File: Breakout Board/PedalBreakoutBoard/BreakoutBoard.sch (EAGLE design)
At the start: 45 parts, among them J7 SMT GUITAR DC JACK, U1 ES_DAISY_SEED_REV4

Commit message: DP-16 - Working on board layout
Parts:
- removed J7: SMT GUITAR DC JACK, Electrosmith-Connectors:GUITAR_DC_JACK
- added PWR: (no value), SparkFun-Connectors:CONN_02
- renumbered R1 to L1, R10 to D21, R11 to D12, R12 to D11, R13 to 8T1, R14 to 8T2, R15 to 8T3, R16 to 8T4, R17 to 8T5, R18 to 8T6, R19 to 8T7, R2 to L2, R20 to 8T8, R3 to L3, R4 to S4, R5 to S3, R6 to S2, R7 to S1, R8 to L4, R9 to D22
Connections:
- net 1P8T_1: now also U1.GPIO31(USB_HS_D+); no longer U1.GPIO24(DAC1_OUT1)
- net 1P8T_2: now also U1.GPIO30(USB_HS_D_-); no longer U1.GPIO25(SAI2_MCLK_B)
- net 1P8T_3: now also U1.GPIO29(SAI2_SCK_B); no longer U1.GPIO26(SAI2_SD_B)
- net 1P8T_4: now also U1.GPIO28(SAI2_FS_B); no longer U1.GPIO27(SAI2_SD_A)
- net 1P8T_5: now also U1.GPIO27(SAI2_SD_A); no longer U1.GPIO28(SAI2_FS_B)
- net 1P8T_6: now also U1.GPIO26(SAI2_SD_B); no longer U1.GPIO29(SAI2_SCK_B)
- net 1P8T_7: now also U1.GPIO25(SAI2_MCLK_B); no longer U1.GPIO30(USB_HS_D_-)
- net 1P8T_8: now also U1.GPIO24(DAC1_OUT1); no longer U1.GPIO31(USB_HS_D+)
- net GND: now also PWR.1; no longer J7.GND
- net N$2: now also PWR.2; no longer J7.PIN

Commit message: DP-16 - Board layout REV-A
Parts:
- removed 1P8T: (no value), SparkFun-Connectors:CONN_09
- removed GPIOS: (no value), SparkFun-Connectors:CONN_07
- removed IN_L, IN_R, LED1, LED2, LED3, LED4, OUT_L, OUT_R, SPST1, SPST2, SPST3, SPST4: (no value), SparkFun-Connectors:CONN_02
- removed POT1, POT2, POT3, POT4, SPDT1, SPDT2: (no value), SparkFun-Connectors:CONN_03
- added 1P8T_GPIO: (no value), SparkFun-Connectors:CONN_08"
- added 1P8T_PWR: (no value), SparkFun-Connectors:CONN_01
- added AUDIO, EX_GND, EX_PWR: (no value), SparkFun-Connectors:CONN_04X2
- added EX_GPIOS: (no value), SparkFun-Connectors:CONN_07
- added LED_GND, LED_GPIO, POT_GND, POT_GPIO, POT_PWR, SPDT_GPIO, SPST_GPIO, SPST_PWR: (no value), SparkFun-Connectors:CONN_04
- added SPDT_PWR: (no value), SparkFun-Connectors:CONN_02
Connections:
- removed net GPIO10: GPIOS.6, U1.GPIO10(SPI1_MISO)
- removed net GPIO11: GPIOS.5, U1.GPIO11(SPI1_MOSI)
- removed net GPIO12: GPIOS.4, U1.GPIO12(I2C1_SCL)
- removed net GPIO13: GPIOS.3, U1.GPIO13(I2C1_SDA)
- removed net GPIO14: GPIOS.2, U1.GPIO14(USART1_TX)
- removed net GPIO15: GPIOS.1, U1.GPIO15(USART1_RX)
- removed net GPIO9: GPIOS.7, U1.GPIO9(SPI1_SCK)
- removed net N$6: L2.2, LED2.1
- removed net N$7: L3.2, LED3.1
- removed net N$8: L4.2, LED4.1
- new net GPIO1: EX_GPIOS.7, U1.GPIO1(USB_HS_ID)
- new net GPIO2: EX_GPIOS.6, U1.GPIO2(SDMMC1_D3)
- new net GPIO3: EX_GPIOS.5, U1.GPIO3(SDMMC1_D2)
- new net GPIO4: EX_GPIOS.4, U1.GPIO4(SDMMC1_D1)
- new net GPIO5: EX_GPIOS.3, U1.GPIO5(SDMMC1_D0)
- new net GPIO6: EX_GPIOS.2, U1.GPIO6(SDMMC1_CMD)
- new net GPIO7: EX_GPIOS.1, U1.GPIO7(SDMMC1_CK)
- new net N$1: L1.2, LED_GPIO.1
- new net N$3: L2.2, LED_GPIO.2
- new net N$4: L3.2, LED_GPIO.3
- net +3V3_A: now also 1P8T_PWR.1, EX_PWR.1, EX_PWR.2, EX_PWR.3, EX_PWR.4, EX_PWR.5, EX_PWR.6, EX_PWR.7, EX_PWR.8, POT_PWR.1, POT_PWR.2, POT_PWR.3, POT_PWR.4, SPDT_PWR.1, SPDT_PWR.2, SPST_PWR.1, SPST_PWR.2, SPST_PWR.3, SPST_PWR.4; no longer 1P8T.9, POT1.1, POT2.1, POT3.1, POT4.1, SPDT1.2, SPDT2.2, SPST1.1, SPST2.1, SPST3.1, SPST4.1
- net 1P8T_1: now also 1P8T_GPIO.1; no longer 1P8T.1
- net 1P8T_2: now also 1P8T_GPIO.2; no longer 1P8T.2
- net 1P8T_3: now also 1P8T_GPIO.3; no longer 1P8T.3
- net 1P8T_4: now also 1P8T_GPIO.4; no longer 1P8T.4
- net 1P8T_5: now also 1P8T_GPIO.5; no longer 1P8T.5
- net 1P8T_6: now also 1P8T_GPIO.6; no longer 1P8T.6
- net 1P8T_7: now also 1P8T_GPIO.7; no longer 1P8T.7
- net 1P8T_8: now also 1P8T_GPIO.8; no longer 1P8T.8
- net GND: now also AUDIO.1, AUDIO.3, AUDIO.5, AUDIO.7, EX_GND.1, EX_GND.2, EX_GND.3, EX_GND.4, EX_GND.5, EX_GND.6, EX_GND.7, EX_GND.8, LED_GND.1, LED_GND.2, LED_GND.3, LED_GND.4, POT_GND.1, POT_GND.2, POT_GND.3, POT_GND.4; no longer IN_L.1, IN_R.1, LED1.2, LED2.2, LED3.2, LED4.2, OUT_L.1, OUT_R.1, POT1.3, POT2.3, POT3.3, POT4.3
- net IN_L: now also AUDIO.2; no longer IN_L.2
- net IN_R: now also AUDIO.4; no longer IN_R.2
- net N$5: now also L4.2, LED_GPIO.4; no longer L1.2, LED1.1
- net OUT_L: now also AUDIO.6; no longer OUT_L.2
- net OUT_R: now also AUDIO.8; no longer OUT_R.2
- net POT1: now also POT_GPIO.1; no longer POT1.2
- net POT2: now also POT_GPIO.2; no longer POT2.2
- net POT3: now also POT_GPIO.3; no longer POT3.2
- net POT4: now also POT_GPIO.4; no longer POT4.2
- net SPDT1_1: now also SPDT_GPIO.4, U1.GPIO12(I2C1_SCL); no longer SPDT1.3, U1.GPIO5(SDMMC1_D0)
- net SPDT1_2: now also SPDT_GPIO.3, U1.GPIO13(I2C1_SDA); no longer SPDT1.1, U1.GPIO6(SDMMC1_CMD)
- net SPDT2_1: now also SPDT_GPIO.2, U1.GPIO14(USART1_TX); no longer SPDT2.3, U1.GPIO7(SDMMC1_CK)
- net SPDT2_2: now also SPDT_GPIO.1, U1.GPIO15(USART1_RX); no longer SPDT2.1, U1.GPIO8(SPI1_NSS)
- net SPST1: now also SPST_GPIO.4, U1.GPIO8(SPI1_NSS); no longer SPST1.2, U1.GPIO1(USB_HS_ID)
- net SPST2: now also SPST_GPIO.3, U1.GPIO9(SPI1_SCK); no longer SPST2.2, U1.GPIO2(SDMMC1_D3)
- net SPST3: now also SPST_GPIO.2, U1.GPIO10(SPI1_MISO); no longer SPST3.2, U1.GPIO3(SDMMC1_D2)
- net SPST4: now also SPST_GPIO.1, U1.GPIO11(SPI1_MOSI); no longer SPST4.2, U1.GPIO4(SDMMC1_D1)
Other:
- moved on the sheet: L1, L2, L3, L4

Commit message: DP-16 - Board layout REV-B
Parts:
- removed 1P8T_GPIO: (no value), SparkFun-Connectors:CONN_08"
- removed 8T1, 8T2, 8T3, 8T4: 10k, SparkFun-Resistors:10KOHM-HORIZ-1/4W-5%
- added HEX_GPIO: (no value), SparkFun-Connectors:CONN_04
- EX_GND, EX_PWR: device SparkFun-Connectors:CONN_04X2 -> SparkFun-Connectors:CONN_04
- EX_GPIOS: device SparkFun-Connectors:CONN_07 -> SparkFun-Connectors:CONN_04
- renumbered 1P8T_PWR to HEX_PWR
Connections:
- removed net 1P8T_1: 1P8T_GPIO.1, 8T1.2, U1.GPIO31(USB_HS_D+)
- removed net 1P8T_2: 1P8T_GPIO.2, 8T2.2, U1.GPIO30(USB_HS_D_-)
- removed net 1P8T_3: 1P8T_GPIO.3, 8T3.2, U1.GPIO29(SAI2_SCK_B)
- removed net 1P8T_4: 1P8T_GPIO.4, 8T4.2, U1.GPIO28(SAI2_FS_B)
- removed net 1P8T_5: 1P8T_GPIO.5, 8T5.2, U1.GPIO27(SAI2_SD_A)
- removed net 1P8T_6: 1P8T_GPIO.6, 8T6.2, U1.GPIO26(SAI2_SD_B)
- removed net 1P8T_7: 1P8T_GPIO.7, 8T7.2, U1.GPIO25(SAI2_MCLK_B)
- removed net 1P8T_8: 1P8T_GPIO.8, 8T8.2, U1.GPIO24(DAC1_OUT1)
- removed net GPIO5: EX_GPIOS.3, U1.GPIO5(SDMMC1_D0)
- removed net GPIO6: EX_GPIOS.2, U1.GPIO6(SDMMC1_CMD)
- removed net GPIO7: EX_GPIOS.1, U1.GPIO7(SDMMC1_CK)
- new net HEX_1: 8T5.2, HEX_GPIO.1, U1.GPIO30(USB_HS_D_-)
- new net HEX_2: 8T6.2, HEX_GPIO.2, U1.GPIO29(SAI2_SCK_B)
- new net HEX_3: 8T7.2, HEX_GPIO.3, U1.GPIO28(SAI2_FS_B)
- new net HEX_4: 8T8.2, HEX_GPIO.4, U1.GPIO27(SAI2_SD_A)
- net +3V3_A: no longer EX_PWR.5, EX_PWR.6, EX_PWR.7, EX_PWR.8
- net GND: no longer 8T1.1, 8T2.1, 8T3.1, 8T4.1, EX_GND.5, EX_GND.6, EX_GND.7, EX_GND.8
- net GPIO1: now also EX_GPIOS.4; no longer EX_GPIOS.7
- net GPIO2: now also EX_GPIOS.3; no longer EX_GPIOS.6
- net GPIO3: now also EX_GPIOS.2; no longer EX_GPIOS.5
- net GPIO4: now also EX_GPIOS.1; no longer EX_GPIOS.4
- net POT1: now also U1.GPIO24(DAC1_OUT1); no longer U1.GPIO23(DAC1_OUT2)
- net POT2: now also U1.GPIO23(DAC1_OUT2); no longer U1.GPIO22(ADC1_INP4)
- net POT3: now also U1.GPIO22(ADC1_INP4); no longer U1.GPIO21(ADC1_INP11)
- net POT4: now also U1.GPIO21(ADC1_INP11); no longer U1.GPIO20(ADC1_INP3)
- net SPDT1_1: now also U1.GPIO11(SPI1_MOSI); no longer U1.GPIO12(I2C1_SCL)
- net SPDT1_2: now also U1.GPIO12(I2C1_SCL); no longer U1.GPIO13(I2C1_SDA)
- net SPDT2_1: now also U1.GPIO13(I2C1_SDA); no longer U1.GPIO14(USART1_TX)
- net SPDT2_2: now also U1.GPIO14(USART1_TX); no longer U1.GPIO15(USART1_RX)
- net SPST1: now also U1.GPIO6(SDMMC1_CMD); no longer U1.GPIO8(SPI1_NSS)
- net SPST2: now also U1.GPIO7(SDMMC1_CK); no longer U1.GPIO9(SPI1_SCK)
- net SPST3: now also U1.GPIO8(SPI1_NSS); no longer U1.GPIO10(SPI1_MISO)
- net SPST4: now also U1.GPIO9(SPI1_SCK); no longer U1.GPIO11(SPI1_MOSI)

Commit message: DP-16 - Working on silkscreen and mounting holes
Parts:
- renumbered 8T5 to H1, 8T6 to H2, 8T7 to H3, 8T8 to H4, U1 to SEED

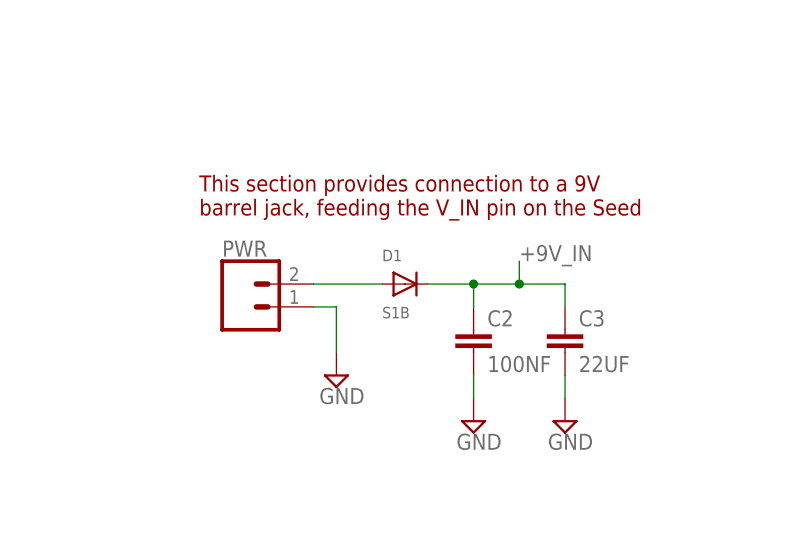
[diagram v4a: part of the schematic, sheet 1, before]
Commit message: DP-16 - Updating to through hole parts
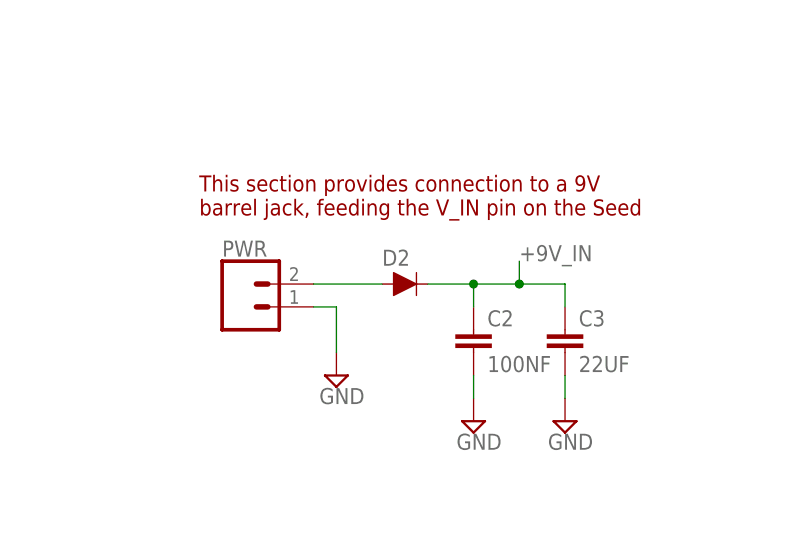
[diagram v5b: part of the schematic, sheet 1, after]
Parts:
- removed D1: S1B, Electrosmith-Semiconductors:S1B
- added D2: 200mA/100V/1V, SparkFun-DiscreteSemi:DIODE-1N4148
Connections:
- net +9V_IN: now also D2.C; no longer D1.C
- net N$2: now also D2.A; no longer D1.A
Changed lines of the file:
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@@
 <part name="C3" library="Electrosmith-Passives" deviceset="C-EU" device="C1206" package3d_urn="urn:adsk.eagle:package:23618/2" value="22UF"/>
 <part name="C2" library="Electrosmith-Passives" deviceset="C-EU" device="C0603" package3d_urn="urn:adsk.eagle:package:23616/2" value="100NF"/>
-<part name="D1" library="Electrosmith-Semiconductors" deviceset="S1B" device=""/>
 <part name="SUPPLY9" library="supply2" library_urn="urn:adsk.eagle:library:372" deviceset="GND" device=""/>
 <part name="SUPPLY10" library="supply2" library_urn="urn:adsk.eagle:library:372" deviceset="GND" device=""/>
@@
 <part name="EX_PWR" library="SparkFun-Connectors" library_urn="urn:adsk.eagle:library:513" deviceset="CONN_04" device="" package3d_urn="urn:adsk.eagle:package:38085/1"/>
 <part name="EX_GND" library="SparkFun-Connectors" library_urn="urn:adsk.eagle:library:513" deviceset="CONN_04" device="" package3d_urn="urn:adsk.eagle:package:38085/1"/>
+<part name="D2" library="SparkFun-DiscreteSemi" library_urn="urn:adsk.eagle:library:514" deviceset="DIODE" device="-1N4148" package3d_urn="urn:adsk.eagle:package:38452/1" value="200mA/100V/1V"/>
 </parts>
 <sheets>
@@
 <attribute name="VALUE" x="82.804" y="15.621" size="1.778" layer="96"/>
 </instance>
-<instance part="D1" gate="G$1" x="73.66" y="25.4" smashed="yes" grouprefs="POWER">
-<attribute name="NAME" x="71.12" y="27.94" size="1.27" layer="95"/>
-<attribute name="VALUE" x="71.12" y="21.59" size="1.27" layer="96"/>
-</instance>
 <instance part="SUPPLY9" gate="GND" x="66.04" y="15.24" smashed="yes" grouprefs="POWER">
 <attribute name="VALUE" x="64.135" y="12.065" size="1.778" layer="96"/>
@@
 <attribute name="VALUE" x="147.32" y="20.066" size="1.778" layer="96" font="vector" rot="R180"/>
 <attribute name="NAME" x="149.86" y="19.812" size="1.778" layer="95" font="vector" rot="R180"/>
+</instance>
+<instance part="D2" gate="G$1" x="73.66" y="25.4" smashed="yes">
+<attribute name="NAME" x="71.12" y="27.432" size="1.778" layer="95" font="vector"/>
 </instance>
 </instances>
@@
 <net name="N$2" class="0">
 <segment>
-<pinref part="D1" gate="G$1" pin="A"/>
 <wire x1="71.12" y1="25.4" x2="63.5" y2="25.4" width="0.1524" layer="91" grouprefs="POWER"/>
 <pinref part="PWR" gate="G$1" pin="2"/>
+<pinref part="D2" gate="G$1" pin="A"/>
 </segment>
 </net>
@@
 <wire x1="86.36" y1="25.4" x2="86.36" y2="27.94" width="0.1524" layer="91" grouprefs="POWER"/>
 <junction x="86.36" y="25.4" grouprefs="POWER"/>
-<pinref part="D1" gate="G$1" pin="C"/>
 <wire x1="76.2" y1="25.4" x2="81.28" y2="25.4" width="0.1524" layer="91" grouprefs="POWER"/>
 <junction x="81.28" y="25.4" grouprefs="POWER"/>
-</segment>
-</net>
+<pinref part="D2" gate="G$1" pin="C"/>
+</segment>
+</net>

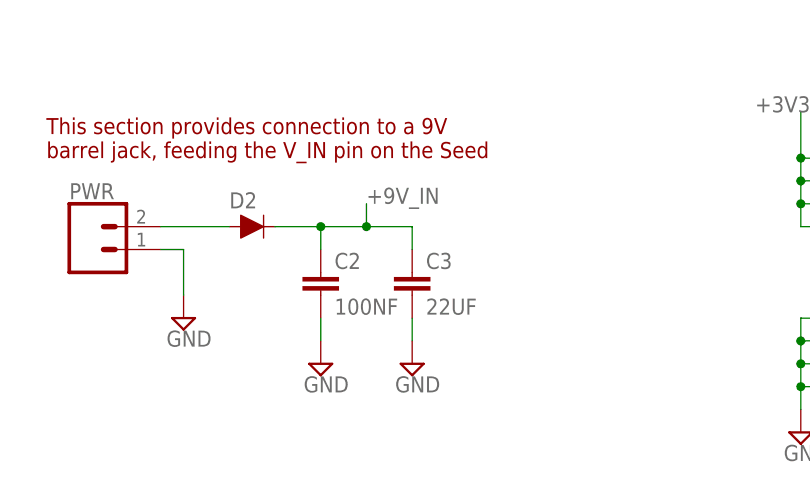
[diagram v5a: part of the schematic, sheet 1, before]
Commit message: DP-16 - Update capacitors to through hole components
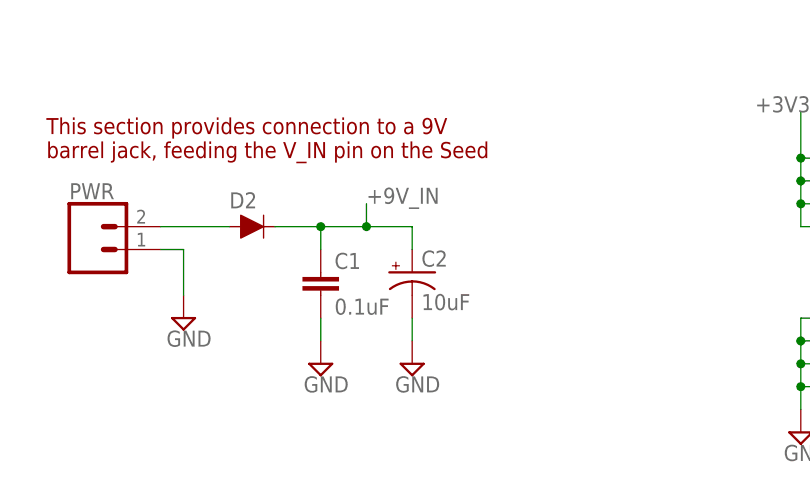
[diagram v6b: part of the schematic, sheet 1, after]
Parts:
- removed C3: 22UF, Electrosmith-Passives:C-EUC1206
- added C1: 0.1uF, SparkFun-Capacitors:0.1UF-KIT-EZ-50V-20%
- C2: value 100NF -> 10uF; device Electrosmith-Passives:C-EUC0603 -> SparkFun-Capacitors:10UF-POLAR-RADIAL-2.5MM-25V-20%
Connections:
- net +9V_IN: now also C1.1, C2.+; no longer C2.1, C3.1
- net GND: now also C1.2, C2.-; no longer C2.2, C3.2
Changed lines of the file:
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@@
 <part name="H3" library="SparkFun-Resistors" library_urn="urn:adsk.eagle:library:532" deviceset="10KOHM" device="-HORIZ-1/4W-5%" package3d_urn="urn:adsk.eagle:package:39658/1" value="10k"/>
 <part name="H4" library="SparkFun-Resistors" library_urn="urn:adsk.eagle:library:532" deviceset="10KOHM" device="-HORIZ-1/4W-5%" package3d_urn="urn:adsk.eagle:package:39658/1" value="10k"/>
-<part name="C3" library="Electrosmith-Passives" deviceset="C-EU" device="C1206" package3d_urn="urn:adsk.eagle:package:23618/2" value="22UF"/>
-<part name="C2" library="Electrosmith-Passives" deviceset="C-EU" device="C0603" package3d_urn="urn:adsk.eagle:package:23616/2" value="100NF"/>
 <part name="SUPPLY9" library="supply2" library_urn="urn:adsk.eagle:library:372" deviceset="GND" device=""/>
 <part name="SUPPLY10" library="supply2" library_urn="urn:adsk.eagle:library:372" deviceset="GND" device=""/>
@@
 <part name="EX_GND" library="SparkFun-Connectors" library_urn="urn:adsk.eagle:library:513" deviceset="CONN_04" device="" package3d_urn="urn:adsk.eagle:package:38085/1"/>
 <part name="D2" library="SparkFun-DiscreteSemi" library_urn="urn:adsk.eagle:library:514" deviceset="DIODE" device="-1N4148" package3d_urn="urn:adsk.eagle:package:38452/1" value="200mA/100V/1V"/>
+<part name="C1" library="SparkFun-Capacitors" library_urn="urn:adsk.eagle:library:510" deviceset="0.1UF" device="-KIT-EZ-50V-20%" package3d_urn="urn:adsk.eagle:package:37428/1" value="0.1uF"/>
+<part name="C2" library="SparkFun-Capacitors" library_urn="urn:adsk.eagle:library:510" deviceset="10UF-POLAR" device="-RADIAL-2.5MM-25V-20%" package3d_urn="urn:adsk.eagle:package:37423/1" value="10uF"/>
 </parts>
 <sheets>
@@
 <attribute name="VALUE" x="180.34" y="67.056" size="1.778" layer="96" font="vector" align="top-center"/>
 </instance>
-<instance part="C3" gate="G$1" x="91.44" y="20.32" smashed="yes" grouprefs="POWER">
-<attribute name="NAME" x="92.964" y="20.701" size="1.778" layer="95"/>
-<attribute name="VALUE" x="92.964" y="15.621" size="1.778" layer="96"/>
-</instance>
-<instance part="C2" gate="G$1" x="81.28" y="20.32" smashed="yes" grouprefs="POWER">
-<attribute name="NAME" x="82.804" y="20.701" size="1.778" layer="95"/>
-<attribute name="VALUE" x="82.804" y="15.621" size="1.778" layer="96"/>
-</instance>
 <instance part="SUPPLY9" gate="GND" x="66.04" y="15.24" smashed="yes" grouprefs="POWER">
 <attribute name="VALUE" x="64.135" y="12.065" size="1.778" layer="96"/>
@@
 <instance part="D2" gate="G$1" x="73.66" y="25.4" smashed="yes">
 <attribute name="NAME" x="71.12" y="27.432" size="1.778" layer="95" font="vector"/>
+</instance>
+<instance part="C1" gate="G$1" x="81.28" y="17.78" smashed="yes">
+<attribute name="NAME" x="82.804" y="20.701" size="1.778" layer="95" font="vector"/>
+<attribute name="VALUE" x="82.804" y="15.621" size="1.778" layer="96" font="vector"/>
+</instance>
+<instance part="C2" gate="G$1" x="91.44" y="20.32" smashed="yes">
+<attribute name="NAME" x="92.456" y="20.955" size="1.778" layer="95" font="vector"/>
+<attribute name="VALUE" x="92.456" y="16.129" size="1.778" layer="96" font="vector"/>
 </instance>
 </instances>
@@
 <net name="GND" class="0">
 <segment>
-<pinref part="C2" gate="G$1" pin="2"/>
 <wire x1="81.28" y1="15.24" x2="81.28" y2="12.7" width="0.1524" layer="91" grouprefs="POWER"/>
 <pinref part="SUPPLY10" gate="GND" pin="GND"/>
-</segment>
-<segment>
-<pinref part="C3" gate="G$1" pin="2"/>
+<pinref part="C1" gate="G$1" pin="2"/>
+</segment>
+<segment>
 <wire x1="91.44" y1="15.24" x2="91.44" y2="12.7" width="0.1524" layer="91" grouprefs="POWER"/>
 <pinref part="SUPPLY11" gate="GND" pin="GND"/>
+<pinref part="C2" gate="G$1" pin="-"/>
 </segment>
 <segment>
@@
 <segment>
 <label x="86.36" y="27.94" size="1.778" layer="95" grouprefs="POWER"/>
-<pinref part="C2" gate="G$1" pin="1"/>
 <wire x1="81.28" y1="22.86" x2="81.28" y2="25.4" width="0.1524" layer="91" grouprefs="POWER"/>
 <wire x1="81.28" y1="25.4" x2="86.36" y2="25.4" width="0.1524" layer="91" grouprefs="POWER"/>
-<pinref part="C3" gate="G$1" pin="1"/>
 <wire x1="86.36" y1="25.4" x2="91.44" y2="25.4" width="0.1524" layer="91" grouprefs="POWER"/>
 <wire x1="91.44" y1="22.86" x2="91.44" y2="25.4" width="0.1524" layer="91" grouprefs="POWER"/>
@@
 <junction x="81.28" y="25.4" grouprefs="POWER"/>
 <pinref part="D2" gate="G$1" pin="C"/>
-</segment>
-</net>
+<pinref part="C1" gate="G$1" pin="1"/>
+<pinref part="C2" gate="G$1" pin="+"/>
+</segment>
+</net>

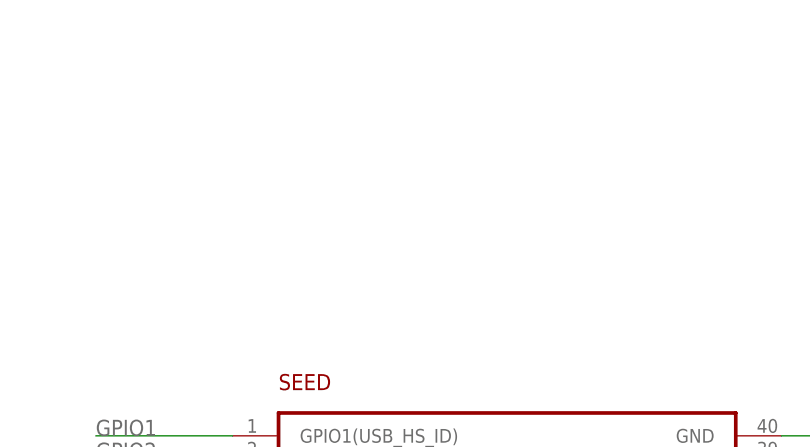
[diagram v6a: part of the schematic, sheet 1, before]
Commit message: DP-16 - Add mounting holes
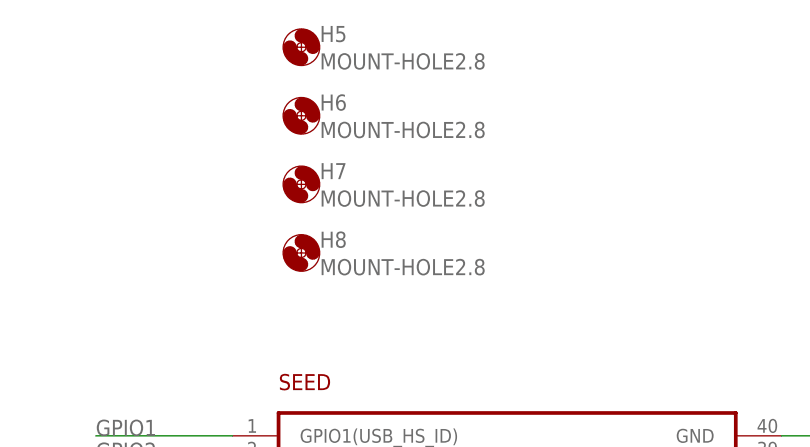
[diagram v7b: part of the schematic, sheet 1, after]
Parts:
- added H5, H6, H7, H8: MOUNT-HOLE2.8, holes:MOUNT-HOLE2.8
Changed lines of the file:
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@@
 <schematic_group name="LED"/>
 <schematic_group name="EXTRA"/>
+<schematic_group name="MOUNT"/>
 </groups>
 <parts>
@@
 <part name="C1" library="SparkFun-Capacitors" library_urn="urn:adsk.eagle:library:510" deviceset="0.1UF" device="-KIT-EZ-50V-20%" package3d_urn="urn:adsk.eagle:package:37428/1" value="0.1uF"/>
 <part name="C2" library="SparkFun-Capacitors" library_urn="urn:adsk.eagle:library:510" deviceset="10UF-POLAR" device="-RADIAL-2.5MM-25V-20%" package3d_urn="urn:adsk.eagle:package:37423/1" value="10uF"/>
+<part name="H5" library="holes" library_urn="urn:adsk.eagle:library:237" deviceset="MOUNT-HOLE" device="2.8" package3d_urn="urn:adsk.eagle:package:14271/1"/>
+<part name="H6" library="holes" library_urn="urn:adsk.eagle:library:237" deviceset="MOUNT-HOLE" device="2.8" package3d_urn="urn:adsk.eagle:package:14271/1"/>
+<part name="H7" library="holes" library_urn="urn:adsk.eagle:library:237" deviceset="MOUNT-HOLE" device="2.8" package3d_urn="urn:adsk.eagle:package:14271/1"/>
+<part name="H8" library="holes" library_urn="urn:adsk.eagle:library:237" deviceset="MOUNT-HOLE" device="2.8" package3d_urn="urn:adsk.eagle:package:14271/1"/>
 </parts>
 <sheets>
@@
 <attribute name="VALUE" x="92.456" y="16.129" size="1.778" layer="96" font="vector"/>
 </instance>
+<instance part="H5" gate="G$1" x="81.28" y="157.48" smashed="yes" grouprefs="MOUNT">
+<attribute name="NAME" x="83.312" y="158.0642" size="1.778" layer="95"/>
+<attribute name="VALUE" x="83.312" y="155.0162" size="1.778" layer="96"/>
+</instance>
+<instance part="H6" gate="G$1" x="81.28" y="149.86" smashed="yes" grouprefs="MOUNT">
+<attribute name="NAME" x="83.312" y="150.4442" size="1.778" layer="95"/>
+<attribute name="VALUE" x="83.312" y="147.3962" size="1.778" layer="96"/>
+</instance>
+<instance part="H7" gate="G$1" x="81.28" y="142.24" smashed="yes" grouprefs="MOUNT">
+<attribute name="NAME" x="83.312" y="142.8242" size="1.778" layer="95"/>
+<attribute name="VALUE" x="83.312" y="139.7762" size="1.778" layer="96"/>
+</instance>
+<instance part="H8" gate="G$1" x="81.28" y="134.62" smashed="yes" grouprefs="MOUNT">
+<attribute name="NAME" x="83.312" y="135.2042" size="1.778" layer="95"/>
+<attribute name="VALUE" x="83.312" y="132.1562" size="1.778" layer="96"/>
+</instance>
 </instances>
